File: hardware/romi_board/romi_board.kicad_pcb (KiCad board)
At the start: 2 copper layers, 107 x 70 mm, 42 parts, among them J1 Conn_01x14, J2 Conn_01x14, J3 Conn_02x06_Odd_Even, Q1 Q_PMOS_DGS, Q2 Q_PMOS_DGS, SW1 SW_SPST, SW2 SW_SPST, U1 Teensy4.0

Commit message: Added switches, optional USB power connector, changed out mouting holes, a few reroutes for SI
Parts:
- removed R10, R11: R_US, Resistor_THT:R_Axial_DIN0309_L9.0mm_D3.2mm_P2.54mm_Vertical
- added H1: MountingHole, MountingHole:MountingHole_2.5mm, F.Cu at (56.4, 124.6)
- added H2: MountingHole, MountingHole:MountingHole_2.5mm, F.Cu at (146.4, 124.6)
- added H3: MountingHole, MountingHole:MountingHole_2.5mm, F.Cu at (79.9, 96.0)
- added H4: MountingHole, MountingHole:MountingHole_2.5mm, F.Cu at (125.6, 96.0)
- added H5: MountingHole, teensy:MountingHole_6mm_passthrough, F.Cu at (76.4, 136.9)
- added H6: MountingHole, teensy:MountingHole_6mm_passthrough, F.Cu at (126.4, 136.9)
- added H7: MountingHole, teensy:MountingHole_6mm_passthrough, F.Cu at (56.4, 149.1)
- added H8: MountingHole, teensy:MountingHole_6mm_passthrough, F.Cu at (146.3, 149.2)
- added J4: USB_B_Micro, Connector_USB:USB_Micro-B_Molex_47346-0001, F.Cu at (52.9, 136.6)
- SW1, SW2: value SW_SPST -> SW_SPDT; footprint Connector_PinHeader_2.54mm:PinHeader_1x02_P2.54mm_Vertical -> teensy:Switch
- moved Q1 16.8 mm to (93.6, 137.6), turned to 180 degrees
- moved SW1 8.92 mm to (78.1, 151.3), turned to 90 degrees
- moved J3 3.17 mm to (73.0, 148.3)
- moved SW2 2.65 mm to (88.2, 151.3)
- moved Q2 1.70 mm to (85.7, 137.6)
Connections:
- SW1 pad 1: GND -> +BATT
- SW2 pad 1: GND -> +BATT
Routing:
- net /RD_OCM: track 90.1 -> 117.6 mm, vias 2 -> 3
- net +BATT: track 32.1 -> 53.4 mm, vias 0 -> 2
- net /LD_OCM: track 112.0 -> 91.3 mm, vias 4 -> 2
- net +VSW: track 46.6 -> 62.1 mm
- net Net-(J4-Pad6): track 0.00 -> 12.6 mm
- net +5V: track 288.7 -> 297.7 mm, vias 7 -> 8
- net Net-(Q1-Pad1): track 21.3 -> 26.9 mm
- net GND: track 36.1 -> 40.9 mm, vias 0 -> 1
- net /RENCB: track 21.6 -> 26.2 mm, vias 1 -> 3
- net Net-(Q2-Pad1): track 24.7 -> 27.5 mm
- net /VBAT_DIV: track 45.0 -> 42.2 mm
- net /RENCA: track 29.6 -> 27.0 mm, vias 1 -> 3
- net /+VMOTOR: track 74.8 -> 73.5 mm
- net /I2C2_SDA: track 95.7 -> 96.4 mm
- net +3V3: track 174.7 -> 174.0 mm
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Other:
- outline, holes or cut-outs redrawn
- board text added: "MOTOR ON>"
- board text added: "PARTS common platform V0.1 2020-06-24 https://github.com/portlandrobotics/common_platform"
- board text added: "PWR ON>"

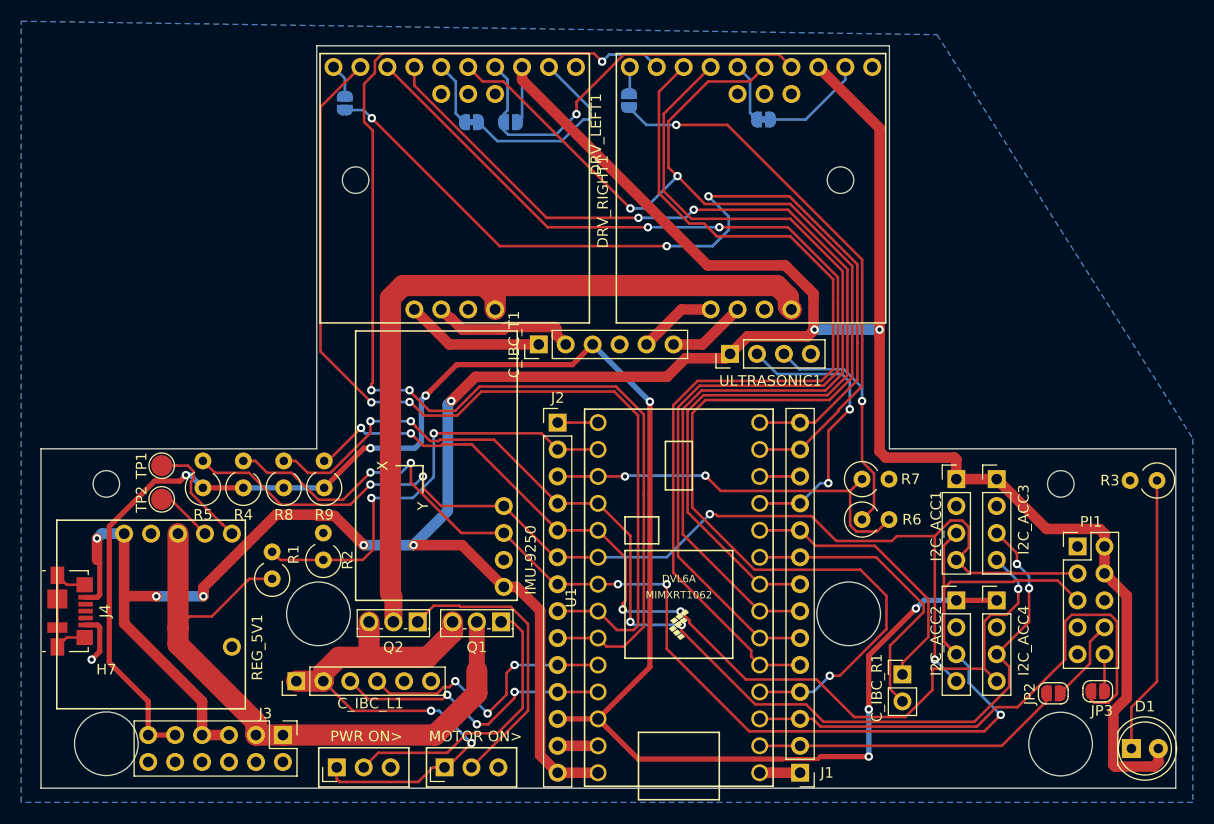
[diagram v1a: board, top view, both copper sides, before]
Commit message: Add power header and filter capacitors to bottom.  Add filter capacitors to top.
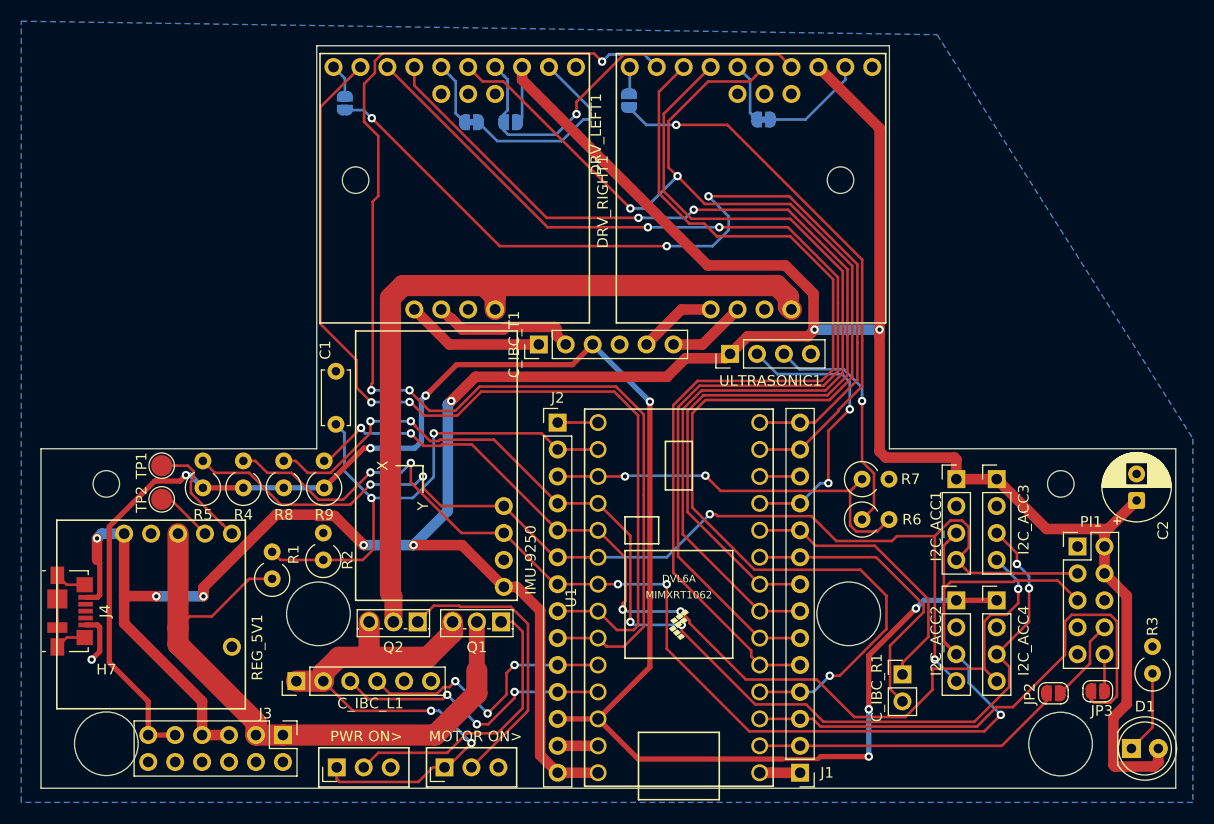
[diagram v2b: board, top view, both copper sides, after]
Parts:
- added C1: 0.1u, Capacitor_THT:C_Disc_D5.0mm_W2.5mm_P5.00mm, F.Cu at (78.0, 119.0)
- added C2: 470u, Capacitor_THT:CP_Radial_D6.3mm_P2.50mm, F.Cu at (153.5, 126.2)
- R1: value R_US -> 2M
- R2: value R_US -> 1M
- R3: value R_US -> 1K
- R4, R5, R8, R9: value R_US -> 4.7K
- R6: value R_Small_US -> 3.3K
- R7: value R_Small_US -> 4.7K
- moved R3 18.2 mm to (155.0, 142.5), turned to 90 degrees
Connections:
- net +3V3 renamed +3.3V
- DRV_LEFT1 pad 15: Net-(DRV_LEFT1-Pad15) -> unconnected-(DRV_LEFT1-Pin_15-Pad15)
- DRV_LEFT1 pad 16: Net-(DRV_LEFT1-Pad16) -> unconnected-(DRV_LEFT1-Pin_16-Pad16)
- DRV_LEFT1 pad 17: Net-(DRV_LEFT1-Pad17) -> unconnected-(DRV_LEFT1-Pin_17-Pad17)
- DRV_RIGHT1 pad 15: Net-(DRV_RIGHT1-Pad15) -> unconnected-(DRV_RIGHT1-Pin_15-Pad15)
- DRV_RIGHT1 pad 16: Net-(DRV_RIGHT1-Pad16) -> unconnected-(DRV_RIGHT1-Pin_16-Pad16)
- DRV_RIGHT1 pad 17: Net-(DRV_RIGHT1-Pad17) -> unconnected-(DRV_RIGHT1-Pin_17-Pad17)
- J4 pad 2: Net-(J4-Pad2) -> unconnected-(J4-D--Pad2)
- J4 pad 3: Net-(J4-Pad3) -> unconnected-(J4-D+-Pad3)
- J4 pad 4: Net-(J4-Pad4) -> unconnected-(J4-ID-Pad4)
- J4 pad 6: Net-(J4-Pad6) -> unconnected-(J4-Shield-Pad6)
- PI1 pad 1: Net-(PI1-Pad1) -> unconnected-(PI1-Pin_1-Pad1)
- PI1 pad 7: Net-(PI1-Pad7) -> unconnected-(PI1-Pin_7-Pad7)
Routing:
- net Net-(D1-K): track 26.3 -> 7.90 mm
- net unconnected-(J4-Shield-Pad6): track 0.00 -> 12.6 mm
- net Net-(J4-Pad6): track 12.6 -> 0.00 mm
- net /VBAT_DIV: track 42.2 -> 50.5 mm
- net +5V: track 297.7 -> 302.3 mm
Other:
- net class Default removed
- net class Med removed
- net class Motor removed
- net class Supply removed
- board text added: "PARTS common platform V1.1 2025-08-29 https://github.com/portlandrobotics/common_platform"
- board text removed: "PARTS common platform V0.1 2020-06-24 https://github.com/portlandrobotics/common_platform"
